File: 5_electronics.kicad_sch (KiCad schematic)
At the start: 1 part, among them J1 Conn_02x20_Odd_Even

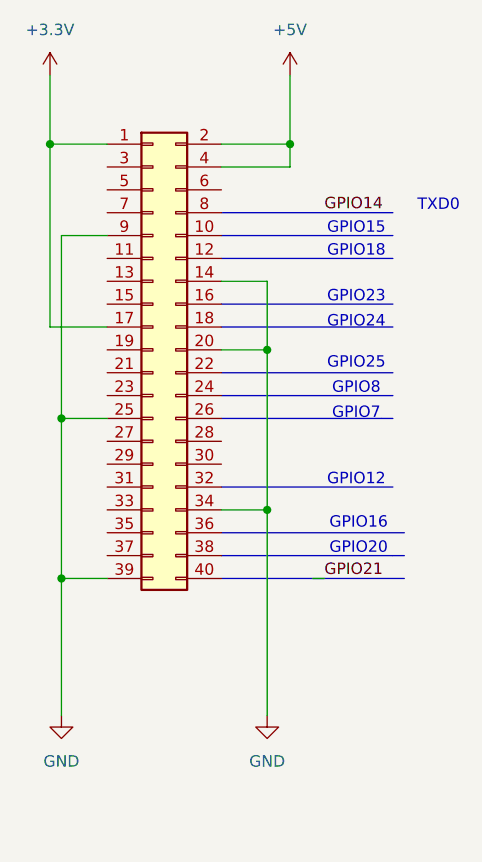
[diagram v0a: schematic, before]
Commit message: Assign footprint
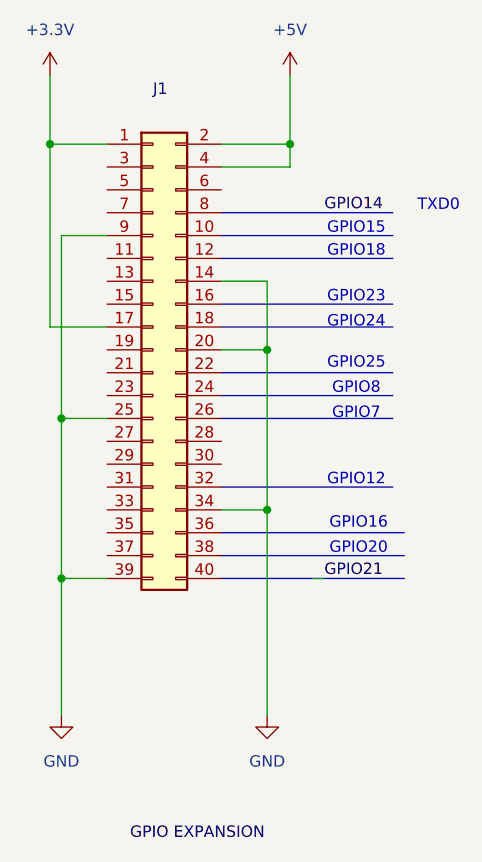
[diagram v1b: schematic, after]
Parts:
- J1: footprint (none) -> Connector_PinHeader_2.54mm:PinHeader_2x20_P2.54mm_Vertical

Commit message: Update
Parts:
- added C1: C_Small, symbol Device:C_Small
- added CAMERA: Conn_01x15, symbol Connector_Generic:Conn_01x15
- added FAN: Conn_01x02, symbol Connector_Generic:Conn_01x02
- added I2C_SENSOR_CONNECTOR, PIR_Sensor, Temperature&Humidity_Sensor: Conn_01x04, symbol Connector_Generic:Conn_01x04
- added J2: Raspberry_Pi_4, symbol Connector:Raspberry_Pi_4
- added R1: R_Small, symbol Device:R_Small
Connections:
- net +3.3V: now also PIR_Sensor.2 (Pin_2)
- net +5V: now also FAN.1 (Pin_1), J2.2 (5V), J2.4 (5V)
- net GND: now also CAMERA.2 (Pin_2), FAN.2 (Pin_2), I2C_SENSOR_CONNECTOR.2 (Pin_2), J2.14 (GND), J2.20 (GND), J2.25 (GND), J2.30 (GND), J2.34 (GND), J2.39 (GND), J2.6 (GND), J2.9 (GND), PIR_Sensor.1 (Pin_1)
- new net +3V3: CAMERA.1 (Pin_1), I2C_SENSOR_CONNECTOR.1 (Pin_1), J2.1 (3V3), J2.17 (3V3)
- new net GPIO_PIR: J2.11 (GPIO17/SPI1_~{CE1})
- new net I2C_SCL: I2C_SENSOR_CONNECTOR.4 (Pin_4), J2.5 (SCL_I2C1/GPIO03)
- new net I2C_SDA: I2C_SENSOR_CONNECTOR.3 (Pin_3), J2.3 (SDA_I2C1/GPIO02)
- new net PIR: PIR_Sensor.4 (Pin_4)
- no-connect marks 0 -> 1

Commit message: Updated
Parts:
- removed C1: C_Small, symbol Device:C_Small
- removed R1: R_Small, symbol Device:R_Small
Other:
- moved on the sheet: CAMERA

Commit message: Updated
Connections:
- net +3V3: now also Temperature&Humidity_Sensor.1 (Pin_1)
- net GND: now also Temperature&Humidity_Sensor.2 (Pin_2)
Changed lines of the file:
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@@
+	(wire
+		(pts
+			(xy 68.58 81.28) (xy 72.39 81.28)
+		)
+		(stroke
+			(width 0)
+			(type default)
+		)
+	)
+	(wire
+		(pts
+			(xy 68.58 83.82) (xy 72.39 83.82)
+		)
+		(stroke
+			(width 0)
+			(type default)
+		)
+	)
 	(wire
 		(pts
@@
 				(justify left)
 				(hide yes)
+			)
+		)
+	)
+	(symbol
+		(lib_id "power:GND")
+		(at 68.58 83.82 0)
+		(unit 1)
+		(exclude_from_sim no)
+		(in_bom yes)
+		(on_board yes)
+		(dnp no)
+		(property "Reference" "#PWR016"
+			(at 68.58 90.17 0)
+			(effects
+				(font
+					(size 1.27 1.27)
+				)
+				(hide yes)
+			)
+		)
+		(property "Value" "GND"
+			(at 68.58 88.9 0)
+			(effects
+				(font
+					(size 1.27 1.27)
+				)
+			)
+		)
+		(property "Footprint" ""
+			(at 68.58 83.82 0)
+			(effects
+				(font
+					(size 1.27 1.27)
+				)
+				(hide yes)
+			)
+		)
+		(property "Datasheet" ""
+			(at 68.58 83.82 0)
+			(effects
+				(font
+					(size 1.27 1.27)
+				)
+				(hide yes)
+			)
+		)
+		(property "Description" "Power symbol creates a global label with name \"GND\" , ground"
+			(at 68.58 83.82 0)
+			(effects
+				(font
+					(size 1.27 1.27)
+				)
+				(hide yes)
+			)
+		)
+		(pin "1"
+		)
+		(instances
+			(project "5_electronics"
+				(path "/b9f81094-eb83-479c-a644-7dc92c1427a8"
+					(reference "#PWR016")
+					(unit 1)
+				)
 			)
 		)
@@
 					(unit 1)
 				)
+			)
+		)
+	)
+	(symbol
+		(lib_id "power:+3V3")
+		(at 68.58 81.28 0)
+		(unit 1)
+		(exclude_from_sim no)
+		(in_bom yes)
+		(on_board yes)
+		(dnp no)
+		(fields_autoplaced yes)
+		(property "Reference" "#PWR015"
+			(at 68.58 85.09 0)
+			(effects
+				(font
+					(size 1.27 1.27)
+				)
+				(hide yes)
+			)
+		)
+		(property "Value" "+3V3"
+			(at 68.58 76.2 0)
+			(effects
+				(font
+					(size 1.27 1.27)
+				)
+			)
+		)
+		(property "Footprint" ""
+			(at 68.58 81.28 0)
+			(effects
+				(font
+					(size 1.27 1.27)
+				)
+				(hide yes)
+			)
+		)
+		(property "Datasheet" ""
+			(at 68.58 81.28 0)
+			(effects
+				(font
+					(size 1.27 1.27)
+				)
+				(hide yes)
+			)
+		)
+		(property "Description" "Power symbol creates a global label with name \"+3V3\""
+			(at 68.58 81.28 0)
+			(effects
+				(font
+					(size 1.27 1.27)
+				)
+				(hide yes)
+			)
+		)
+		(pin "1"
+		)
+		(instances
+			(project "5_electronics"
+				(path "/b9f81094-eb83-479c-a644-7dc92c1427a8"
+					(reference "#PWR015")
+					(unit 1)
+				)

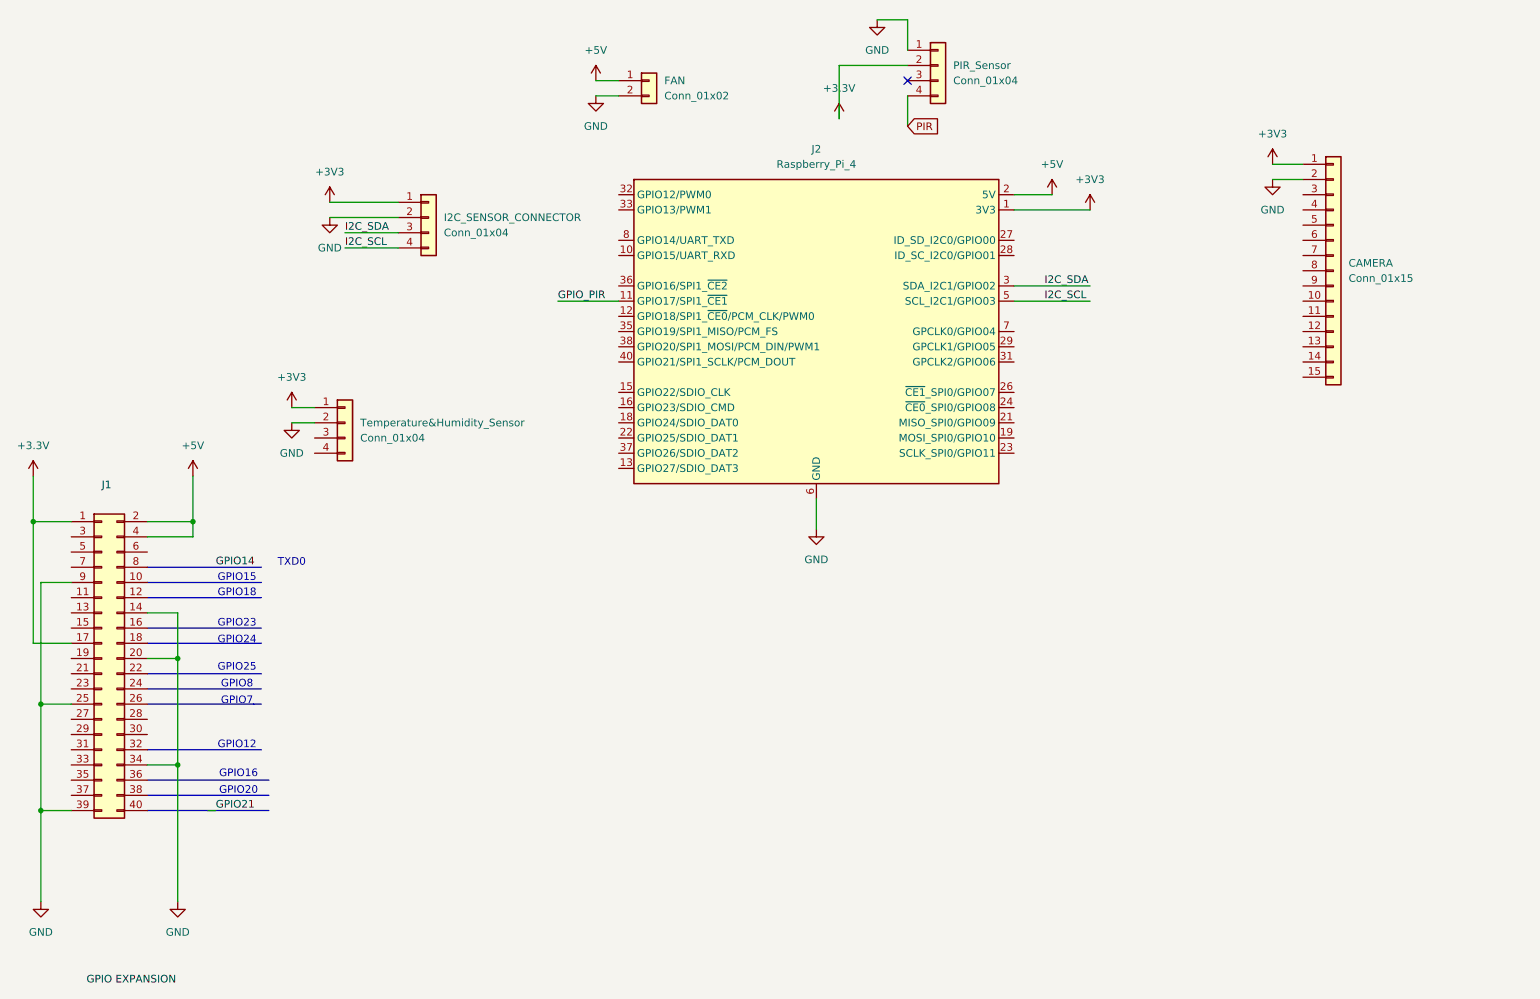
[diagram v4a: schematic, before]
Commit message: E-paper added
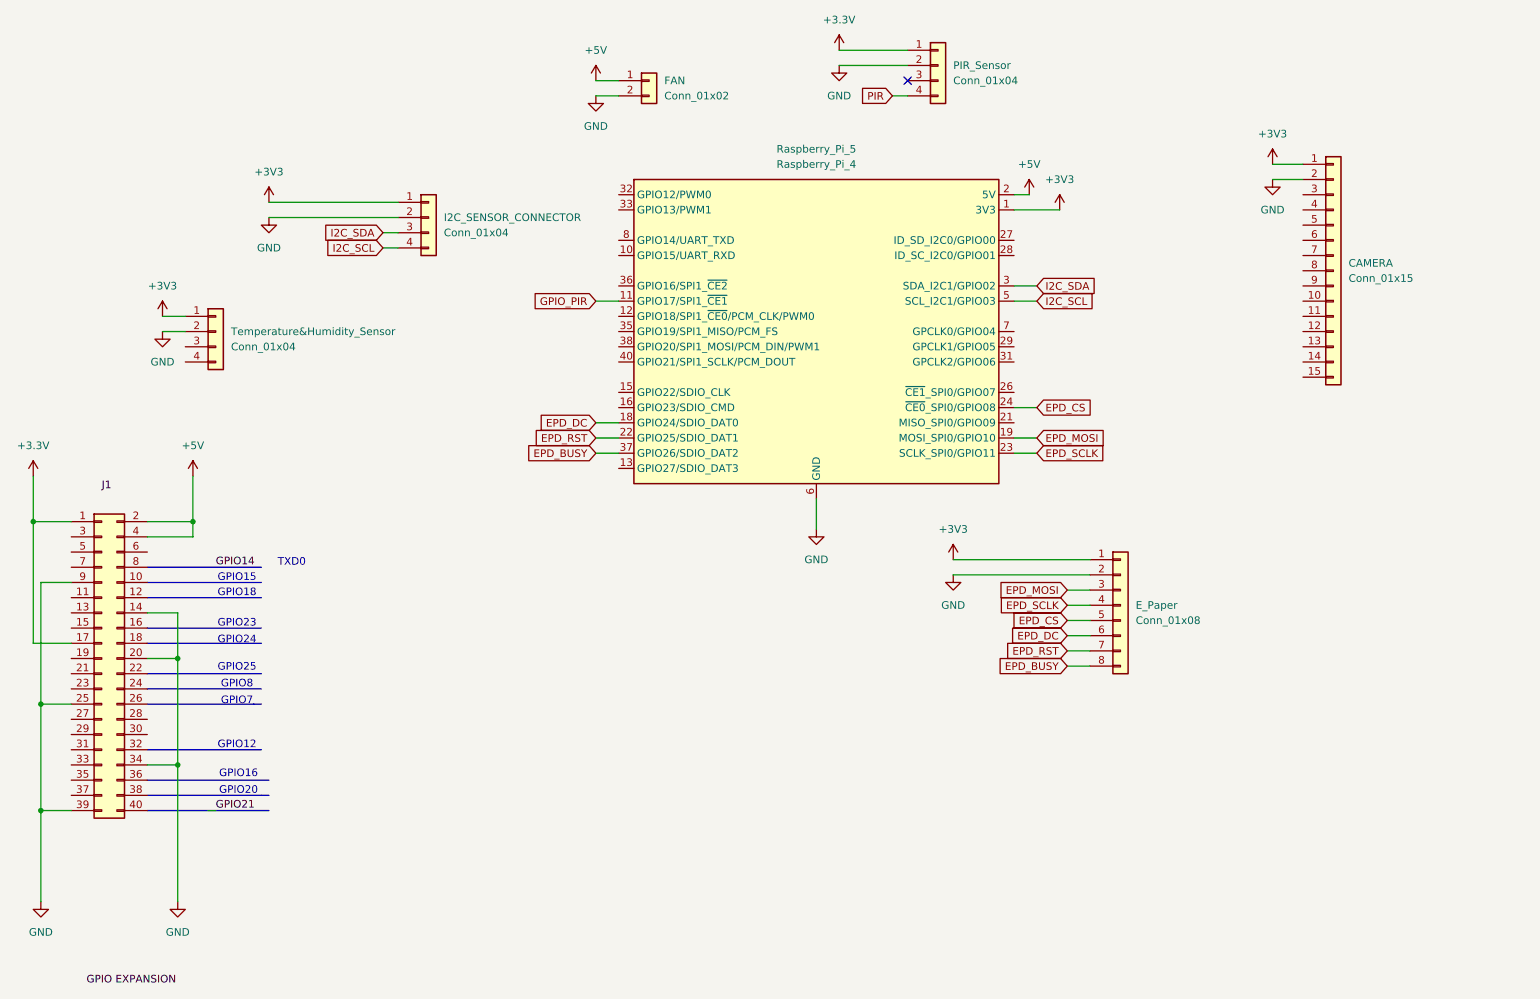
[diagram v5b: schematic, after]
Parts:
- added E_Paper: Conn_01x08, symbol Connector_Generic:Conn_01x08
- renumbered J2 to Raspberry_Pi_5
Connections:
- net +3.3V: now also PIR_Sensor.1 (Pin_1); no longer PIR_Sensor.2 (Pin_2)
- net +3V3: now also E_Paper.1 (Pin_1)
- net GND: now also PIR_Sensor.2 (Pin_2), E_Paper.2 (Pin_2); no longer PIR_Sensor.1 (Pin_1)
- net EPD_DC: now reaches Raspberry_Pi_5.18 (GPIO24/SDIO_DAT0)
- net EPD_DC: now also E_Paper.6 (Pin_6)
- net EPD_MOSI: now reaches Raspberry_Pi_5.19 (MOSI_SPI0/GPIO10)
- net EPD_MOSI: now also E_Paper.3 (Pin_3)
- net EPD_RST: now reaches Raspberry_Pi_5.22 (GPIO25/SDIO_DAT1)
- net EPD_RST: now also E_Paper.7 (Pin_7)
- net EPD_SCLK: now reaches Raspberry_Pi_5.23 (SCLK_SPI0/GPIO11)
- net EPD_SCLK: now also E_Paper.4 (Pin_4)
- net EPD_CS: now reaches Raspberry_Pi_5.24 (~{CE0}_SPI0/GPIO08)
- net EPD_CS: now also E_Paper.5 (Pin_5)
- net EPD_BUSY: now reaches Raspberry_Pi_5.37 (GPIO26/SDIO_DAT2)
- net EPD_BUSY: now also E_Paper.8 (Pin_8)
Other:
- moved on the sheet: Temperature&Humidity_Sensor

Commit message: Temperature & Humidity sensor connected
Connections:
- net I2C_SCL: now also Temperature&Humidity_Sensor.4 (Pin_4)
- net I2C_SDA: now also Temperature&Humidity_Sensor.3 (Pin_3)
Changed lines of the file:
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@@
+	(wire
+		(pts
+			(xy 48.26 73.66) (xy 50.8 73.66)
+		)
+		(stroke
+			(width 0)
+			(type default)
+		)
+	)
 	(wire
 		(pts
@@
 	(wire
 		(pts
-			(xy 46.99 66.04) (xy 50.8 66.04)
-		)
-		(stroke
-			(width 0)
-			(type default)
-		)
-	)
-	(wire
-		(pts
-			(xy 46.99 68.58) (xy 50.8 68.58)
+			(xy 34.29 66.04) (xy 50.8 66.04)
+		)
+		(stroke
+			(width 0)
+			(type default)
+		)
+	)
+	(wire
+		(pts
+			(xy 34.29 68.58) (xy 50.8 68.58)
 		)
 		(stroke
@@
 	(wire
 		(pts
-			(xy 64.77 49.53) (xy 86.36 49.53)
+			(xy 69.85 49.53) (xy 86.36 49.53)
 		)
 		(stroke
@@
 	(wire
 		(pts
+			(xy 48.26 71.12) (xy 50.8 71.12)
+		)
+		(stroke
+			(width 0)
+			(type default)
+		)
+	)
+	(wire
+		(pts
 			(xy 198.12 124.46) (xy 201.93 124.46)
 		)
@@
 	(wire
 		(pts
-			(xy 64.77 46.99) (xy 86.36 46.99)
+			(xy 69.85 46.99) (xy 86.36 46.99)
 		)
 		(stroke
@@
 		)
 	)
+	(global_label "I2C_SDA"
+		(shape input)
+		(at 48.26 71.12 180)
+		(fields_autoplaced yes)
+		(effects
+			(font
+				(size 1.27 1.27)
+			)
+			(justify right)
+		)
+		(property "Intersheetrefs" "${INTERSHEET_REFS}"
+			(at 37.6548 71.12 0)
+			(effects
+				(font
+					(size 1.27 1.27)
+				)
+				(justify right)
+				(hide yes)
+			)
+		)
+	)
 	(global_label "PIR"
 		(shape input)
@@
 		)
 	)
+	(global_label "I2C_SCL"
+		(shape input)
+		(at 48.26 73.66 180)
+		(fields_autoplaced yes)
+		(effects
+			(font
+				(size 1.27 1.27)
+			)
+			(justify right)
+		)
+		(property "Intersheetrefs" "${INTERSHEET_REFS}"
+			(at 37.7153 73.66 0)
+			(effects
+				(font
+					(size 1.27 1.27)
+				)
+				(justify right)
+				(hide yes)
+			)
+		)
+	)
 	(global_label "EPD_RST"
 		(shape input)
@@
 	(symbol
 		(lib_id "power:GND")
-		(at 46.99 68.58 0)
+		(at 34.29 68.58 0)
 		(unit 1)
 		(exclude_from_sim no)
@@
 		(dnp no)
 		(property "Reference" "#PWR016"
-			(at 46.99 74.93 0)
+			(at 34.29 74.93 0)
 			(effects
 				(font
@@
 		)
 		(property "Value" "GND"
-			(at 46.99 73.66 0)
+			(at 34.29 73.66 0)
 			(effects
 				(font
@@
 		)
 		(property "Footprint" ""
-			(at 46.99 68.58 0)
+			(at 34.29 68.58 0)
 			(effects
 				(font
@@
 		)
 		(property "Datasheet" ""
-			(at 46.99 68.58 0)
+			(at 34.29 68.58 0)
 			(effects
 				(font
@@
 		)
 		(property "Description" "Power symbol creates a global label with name \"GND\" , ground"
-			(at 46.99 68.58 0)
+			(at 34.29 68.58 0)
 			(effects
 				(font
@@
 	(symbol
 		(lib_id "power:+3V3")
-		(at 64.77 46.99 0)
+		(at 69.85 46.99 0)
 		(unit 1)
 		(exclude_from_sim no)
@@
 		(fields_autoplaced yes)
 		(property "Reference" "#PWR013"
-			(at 64.77 50.8 0)
+			(at 69.85 50.8 0)
 			(effects
 				(font
@@
 		)
 		(property "Value" "+3V3"
-			(at 64.77 41.91 0)
+			(at 69.85 41.91 0)
 			(effects
 				(font
@@
 		)
 		(property "Footprint" ""
-			(at 64.77 46.99 0)
+			(at 69.85 46.99 0)
 			(effects
 				(font
@@
 		)
 		(property "Datasheet" ""
-			(at 64.77 46.99 0)
+			(at 69.85 46.99 0)
 			(effects
 				(font
@@
 		)
 		(property "Description" "Power symbol creates a global label with name \"+3V3\""
-			(at 64.77 46.99 0)
+			(at 69.85 46.99 0)
 			(effects
 				(font
@@
 	(symbol
 		(lib_id "power:+3V3")
-		(at 46.99 66.04 0)
+		(at 34.29 66.04 0)
 		(unit 1)
 		(exclude_from_sim no)
@@
 		(fields_autoplaced yes)
 		(property "Reference" "#PWR015"
-			(at 46.99 69.85 0)
+			(at 34.29 69.85 0)
 			(effects
 				(font
@@
 		)
 		(property "Value" "+3V3"
-			(at 46.99 60.96 0)
+			(at 34.29 60.96 0)
 			(effects
 				(font
@@
 		)
 		(property "Footprint" ""
-			(at 46.99 66.04 0)
+			(at 34.29 66.04 0)
 			(effects
 				(font
@@
 		)
 		(property "Datasheet" ""
-			(at 46.99 66.04 0)
+			(at 34.29 66.04 0)
 			(effects
 				(font
@@
 		)
 		(property "Description" "Power symbol creates a global label with name \"+3V3\""
-			(at 46.99 66.04 0)
+			(at 34.29 66.04 0)
 			(effects
 				(font
@@
 	(symbol
 		(lib_id "power:GND")
-		(at 64.77 49.53 0)
+		(at 69.85 49.53 0)
 		(unit 1)
 		(exclude_from_sim no)
@@
 		(dnp no)
 		(property "Reference" "#PWR014"
-			(at 64.77 55.88 0)
+			(at 69.85 55.88 0)
 			(effects
 				(font
@@
 		)
 		(property "Value" "GND"
-			(at 64.77 54.61 0)
+			(at 69.85 54.61 0)
 			(effects
 				(font
@@
 		)
 		(property "Footprint" ""
-			(at 64.77 49.53 0)
+			(at 69.85 49.53 0)
 			(effects
 				(font
@@
 		)
 		(property "Datasheet" ""
-			(at 64.77 49.53 0)
+			(at 69.85 49.53 0)
 			(effects
 				(font
@@
 		)
 		(property "Description" "Power symbol creates a global label with name \"GND\" , ground"
-			(at 64.77 49.53 0)
-			(effects
-				(font
+			(at 69.85 49.53 0)
+			(effects
+				(font

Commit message: Updated
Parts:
- added BT1: Battery_Cell, symbol Device:Battery_Cell
- added INA219_Sensor: Conn_01x06, symbol Connector_Generic:Conn_01x06
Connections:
- net +3V3: now also INA219_Sensor.1 (Pin_1)
- net GND: now also INA219_Sensor.2 (Pin_2)
- net I2C_SCL: now also INA219_Sensor.4 (Pin_4)
- net I2C_SDA: now also INA219_Sensor.3 (Pin_3)
- new net BAT+: BT1.1 (+), INA219_Sensor.5 (Pin_5)
- new net BAT-: BT1.2 (-)
- new net SYS_PWR: INA219_Sensor.6 (Pin_6)
